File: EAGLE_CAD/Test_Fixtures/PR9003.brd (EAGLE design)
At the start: 96 x 93.5 mm, 3 parts

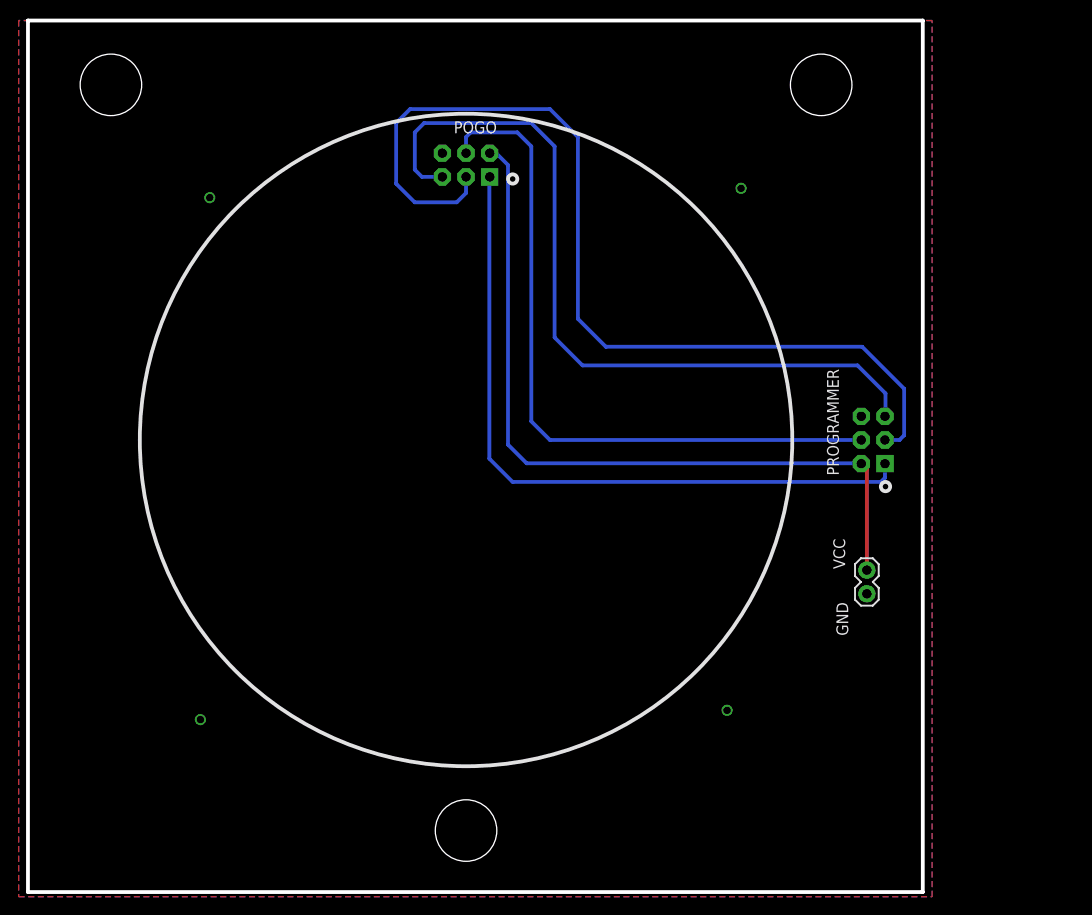
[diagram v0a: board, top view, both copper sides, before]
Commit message: 9003 updates
added test points for all locations
rerouted vcc so DUT can only be programed when the POT is in the on position.

to do:
route traces
add package for push button
add push button
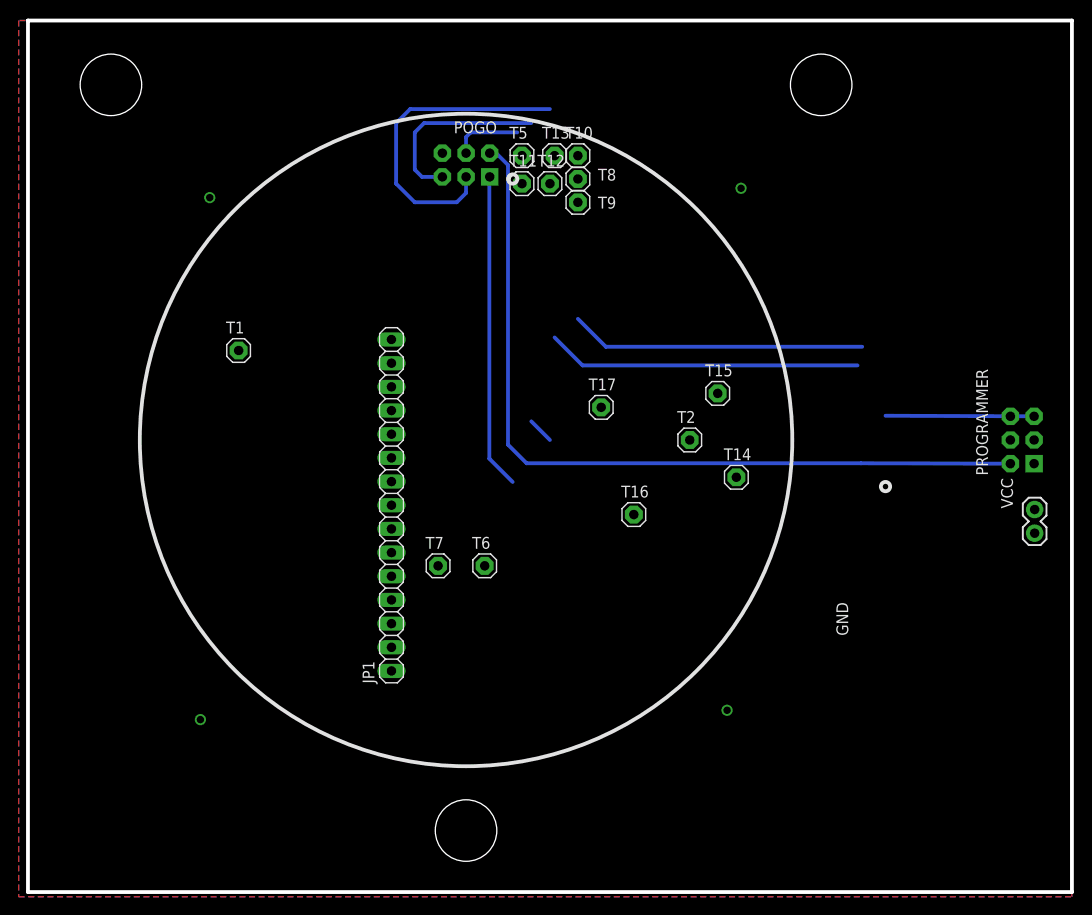
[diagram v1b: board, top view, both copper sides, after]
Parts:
- added JP1: (no value), adafruit:1X15
- added T1, T10, T11, T12, T13, T14, T15, T16, T17, T2, T5, T6, T7, T8, T9: (no value), adafruit:1X01
- moved VCC 19.1 mm to (96.0, 25.0)
- moved PROGRAMMER 16.0 mm to (94.7, 35.0)
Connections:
- new net N$1: JP1.1, T1.1
- new net N$10: JP1.10, T12.1
- new net N$11: JP1.11, T13.1
- new net N$12: JP1.12, T14.1
- new net N$13: T15.1, VCC.2
- new net N$14: JP1.14, T16.1
- new net N$15: JP1.13, T17.1
- new net N$16: JP1.15
- new net N$2: JP1.2, T2.1
- new net N$3: JP1.3, T5.1
- new net N$4: JP1.4, T6.1
- new net N$5: JP1.5, T7.1
- new net N$6: JP1.6, T8.1
- new net N$7: JP1.7, T9.1
- new net N$8: JP1.8, T10.1
- new net N$9: JP1.9, T11.1
- net VCC: no longer VCC.2
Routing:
- net MOSI: track 75.3 -> 10.3 mm
- net MISO: track 75.4 -> 33.8 mm
- net SCK: track 103.2 -> 65.8 mm
- net RESET: track 84.7 -> 69.9 mm
- net VCC: track 82.9 -> 87.2 mm
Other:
- board size 96 x 93.5 mm -> 112 x 93.5 mm

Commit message: PR9003
Routed test point connections
Added push button to library and PCB (https://www.digikey.com/product-detail/en/c-k/D6C40-F2-LFS/401-1985-ND/1466342)

Push button is wired to be used with an RPI pin that should be set high with an internal pull up. Button press will trigger an active low state. Probably need to use the Wiring PiC library.  This will reduce parts needed and eliminate the need to bring 3.3V to the test board.
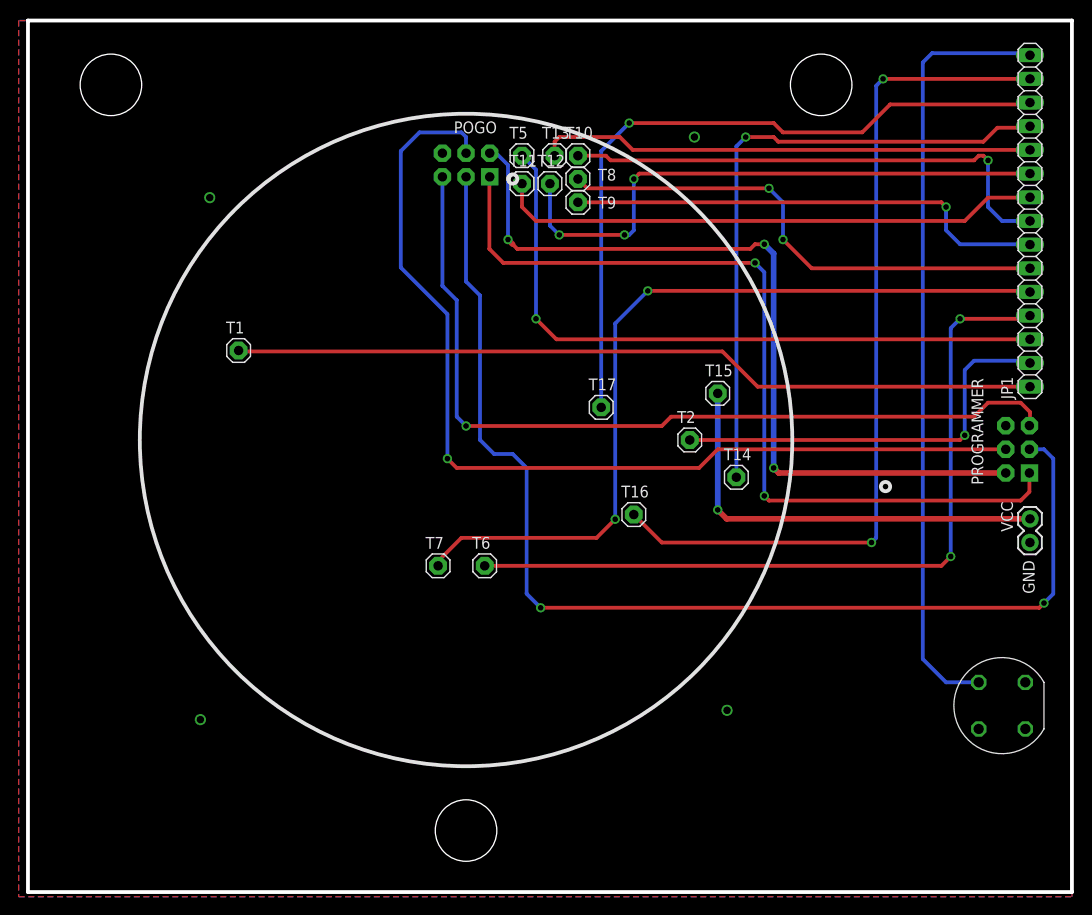
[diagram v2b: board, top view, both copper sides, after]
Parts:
- added U$1: C&K_D6C_SWITCH, PR_Parts_Library:C&K_D6C_SWITCH
- moved JP1 75.0 mm to (95.5, 58.5)
- moved PROGRAMMER 1.12 mm to (94.2, 34.0)
- moved VCC 1.12 mm to (95.5, 24.0)
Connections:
- net GND: now also U$1.P$1
- net N$16: now also U$1.P$3
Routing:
- net MOSI: track 10.3 -> 106.0 mm, vias 0 -> 1
- net N$14: track 0.00 -> 92.8 mm, vias 0 -> 2
- net N$5: track 0.00 -> 88.4 mm, vias 0 -> 2
- net N$1: track 0.00 -> 86.5 mm
- net N$4: track 0.00 -> 84.0 mm, vias 0 -> 2
- net N$16: track 0.00 -> 83.0 mm
- net N$15: track 0.00 -> 76.5 mm, vias 0 -> 1
- net N$3: track 0.00 -> 72.0 mm, vias 0 -> 1
- net N$12: track 0.00 -> 68.3 mm, vias 0 -> 1
- net N$10: track 0.00 -> 62.4 mm, vias 0 -> 3
- net MISO: track 33.8 -> 93.4 mm, vias 0 -> 2
- net N$9: track 0.00 -> 58.7 mm
- net SCK: track 65.8 -> 123.8 mm, vias 0 -> 2
- net N$6: track 0.00 -> 54.8 mm, vias 0 -> 2
- net N$8: track 0.00 -> 54.7 mm, vias 0 -> 1
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
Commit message: PR9003 Updates
Updated masks
Added naming for GPIO breakout
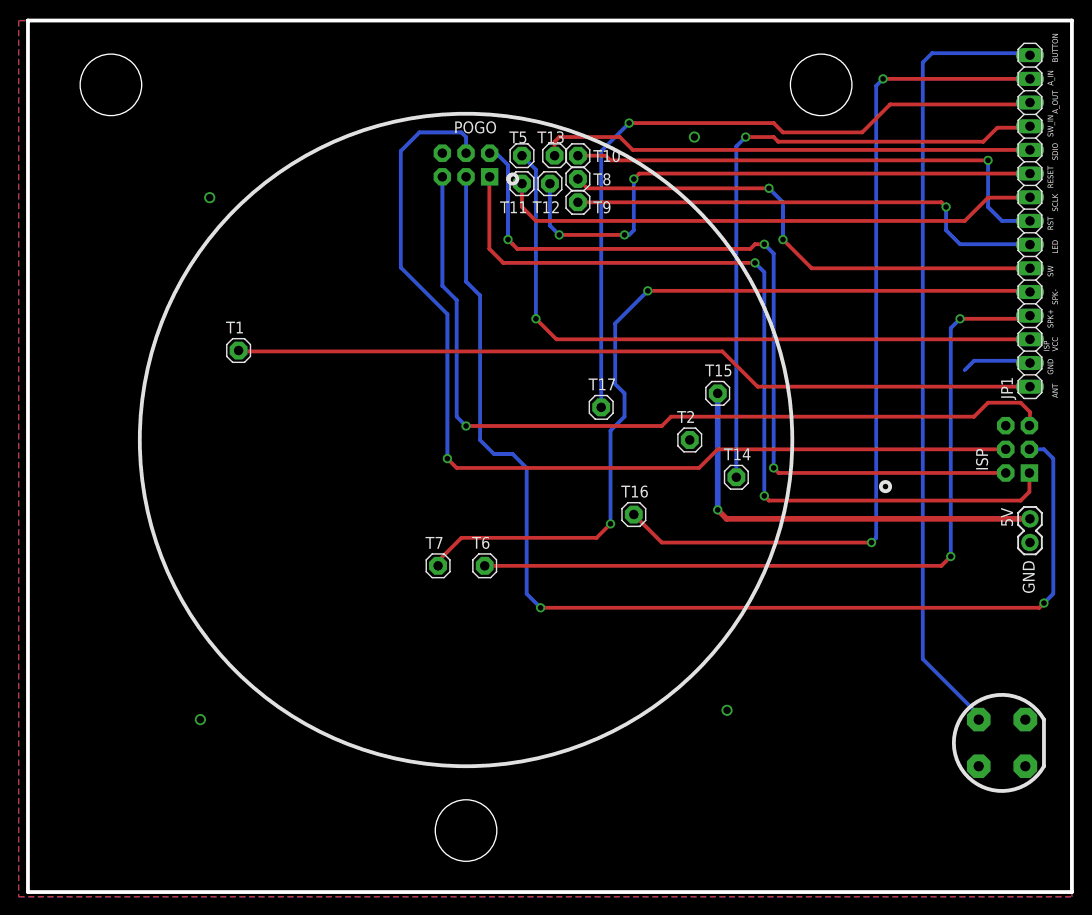
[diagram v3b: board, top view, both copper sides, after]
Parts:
- moved U$1 4.00 mm to (92.5, 2.50)
- renumbered PROGRAMMER to ISP, VCC to 5V
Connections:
- removed net N$2: JP1.2, T2.1
- net GND: now also JP1.2, T2.1
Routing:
- net N$2: track 44.2 -> 0.00 mm, vias 1 -> 0
- net GND: track 0.00 -> 7.17 mm
- net N$16: track 83.0 -> 85.0 mm
- net N$5: track 88.4 -> 89.2 mm
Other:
- board text added: "ANT"
- board text added: "A_IN"
- board text added: "A_OUT"
- board text added: "BUTTON"
- board text added: "ISP VCC"
- board text added: "LED"
- board text added: "RESET"
- board text added: "RST"
- board text added: "SCLK"
- board text added: "SDIO"
- board text added: "SPK+"
- board text added: "SPK-"
- board text added: "SW"
- board text added: "SW_IN"
